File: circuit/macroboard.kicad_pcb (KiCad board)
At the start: 2 copper layers, 89 x 99 mm, 88 parts, among them SW1 CherryMX, SW10 CherryMX, SW11 CherryMX, SW12 CherryMX, SW13 SW_Push, SW14 CherryMX, SW15 SW_SPDT, SW16 SW_SPDT, SW2 CherryMX, SW3 CherryMX, SW4 CherryMX, SW5 CherryMX, SW6 CherryMX, SW7 CherryMX, SW8 CherryMX, SW9 CherryMX, U1 ATmega32U4-A

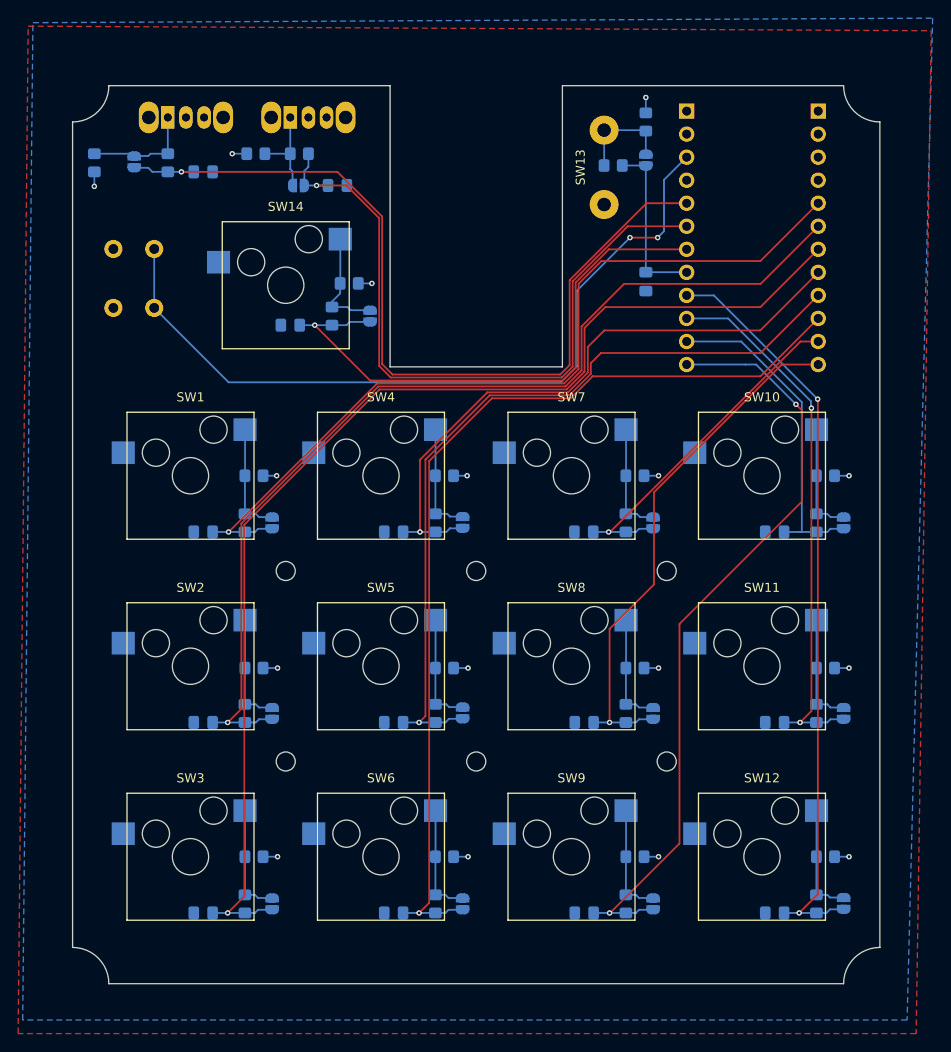
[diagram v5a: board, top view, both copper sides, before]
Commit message: fix wrong pin distance on Arduino micro footprint
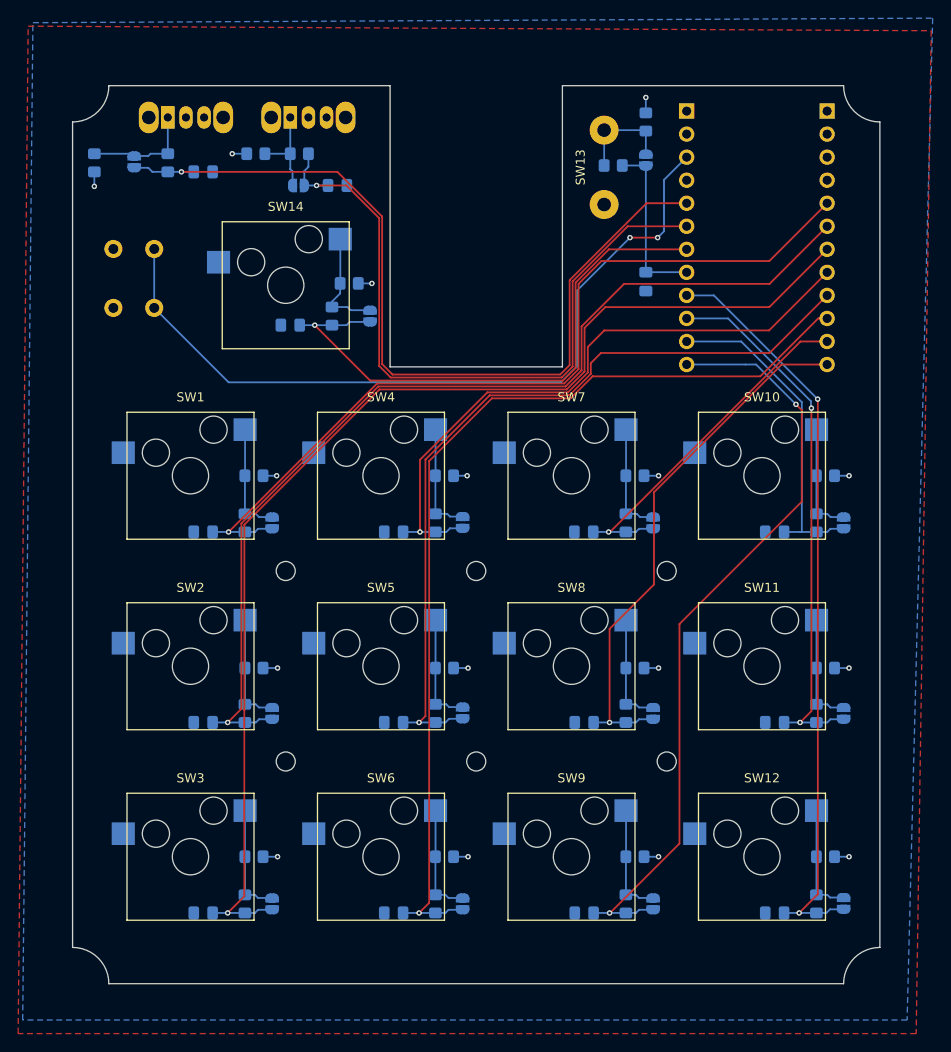
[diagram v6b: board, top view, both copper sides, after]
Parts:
- moved U1 0.98 mm to (150.2, 39.7)
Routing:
- net /KEY8: track 58.1 -> 59.0 mm
- net /KEY6: track 106.4 -> 107.4 mm
- net /KEY5: track 87.5 -> 88.5 mm
- net /KEY7: track 38.5 -> 39.5 mm
- net /KEY2: track 109.2 -> 110.2 mm
- net /KEY3: track 128.9 -> 129.9 mm
- net /KEY1: track 92.2 -> 93.2 mm
- net /KEY4: track 68.8 -> 69.8 mm

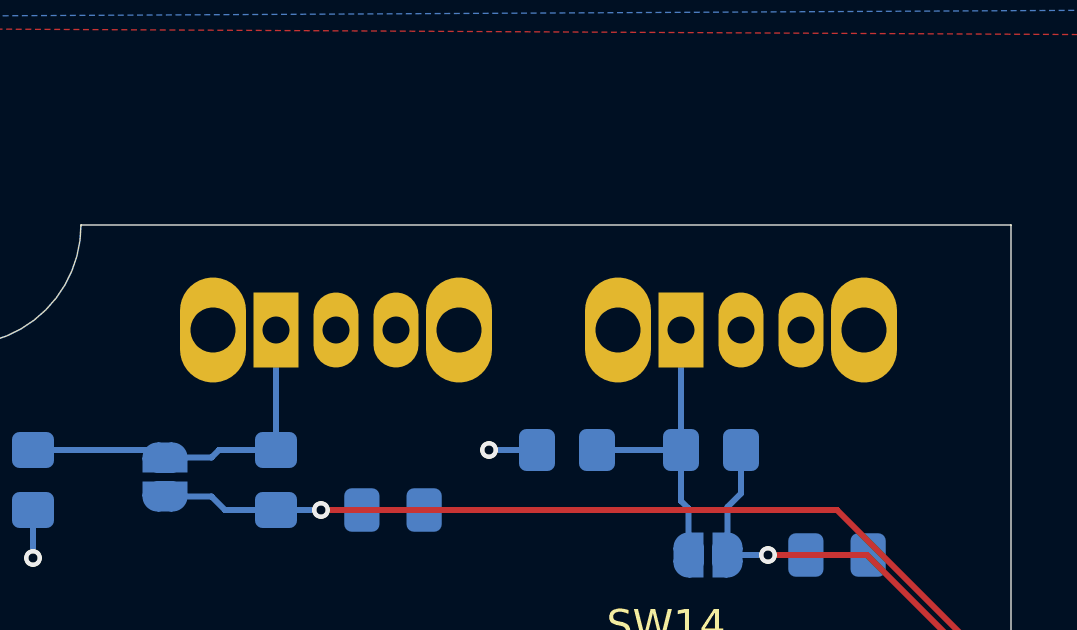
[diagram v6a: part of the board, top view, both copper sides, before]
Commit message: improve switch positioning
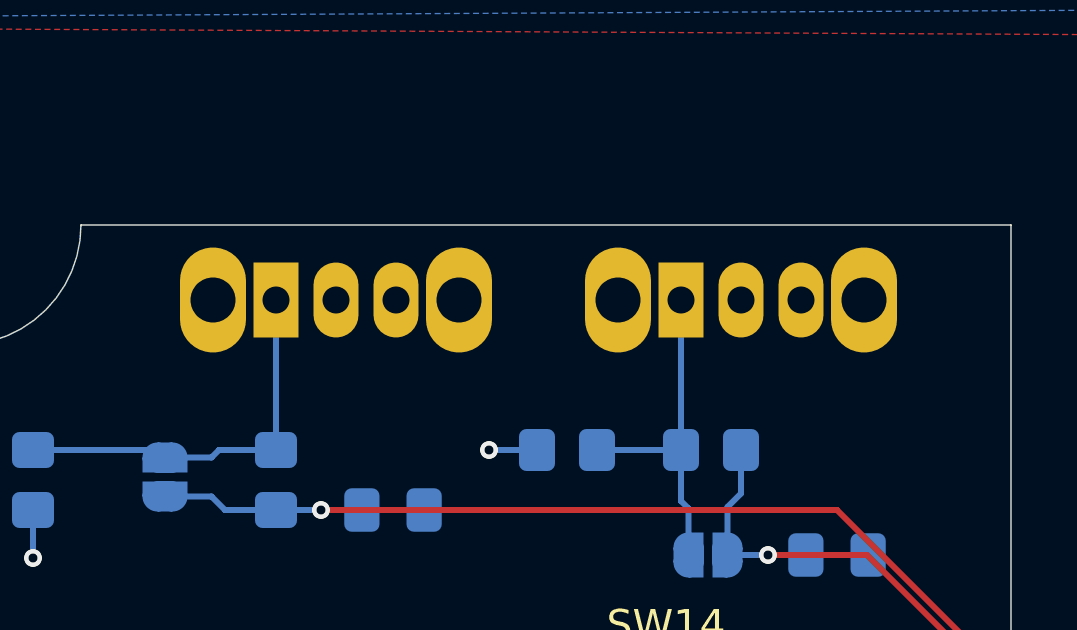
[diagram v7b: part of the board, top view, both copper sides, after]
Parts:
- moved SW15 1.00 mm to (91.0, 39.5)
- moved SW16 1.00 mm to (77.5, 39.5)
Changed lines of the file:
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@@
 	(generator_version "9.0")
 	(general
-		(thickness 1.69)
+		(thickness 1.6)
 		(legacy_teardrops no)
 	)
@@
 			(layer "dielectric 1"
 				(type "core")
-				(thickness 1.6)
+				(thickness 1.51)
 				(material "FR4")
 				(epsilon_r 4.5)
@@
 	(footprint "Button_Switch_THT:SW_Slide_SPDT_Angled_CK_OS102011MA1Q"
 		(layer "B.Cu")
-		(at 77.5 40.5)
+		(at 77.5 39.5)
 		(descr "CuK miniature slide switch, OS series, SPDT, right angle, http://www.ckswitches.com/media/1428/os.pdf")
 		(tags "switch SPDT")
@@
 	(footprint "Button_Switch_THT:SW_Slide_SPDT_Angled_CK_OS102011MA1Q"
 		(layer "B.Cu")
-		(at 91 40.5)
+		(at 91 39.5)
 		(descr "CuK miniature slide switch, OS series, SPDT, right angle, http://www.ckswitches.com/media/1428/os.pdf")
 		(tags "switch SPDT")
